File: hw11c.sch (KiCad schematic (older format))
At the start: 68 parts, among them Q1 KX-7_12MHZ, SW1 BUTT1, SW2 BUTT2, X1 ~RESET, X10 PIO2.8, X11 PIO1.4, X12 ADC3, X13 PIO0.8, X14 PIO0.9, X15 MAT0, X16 PIO0.6, X17 PIO0.7, X2 SWCLK, X3 SWDIO, X4 SSEL1, X5 SCK1, X6 MISO1, X7 MOSI1, X8 PIO2.6, X9 PIO2.7

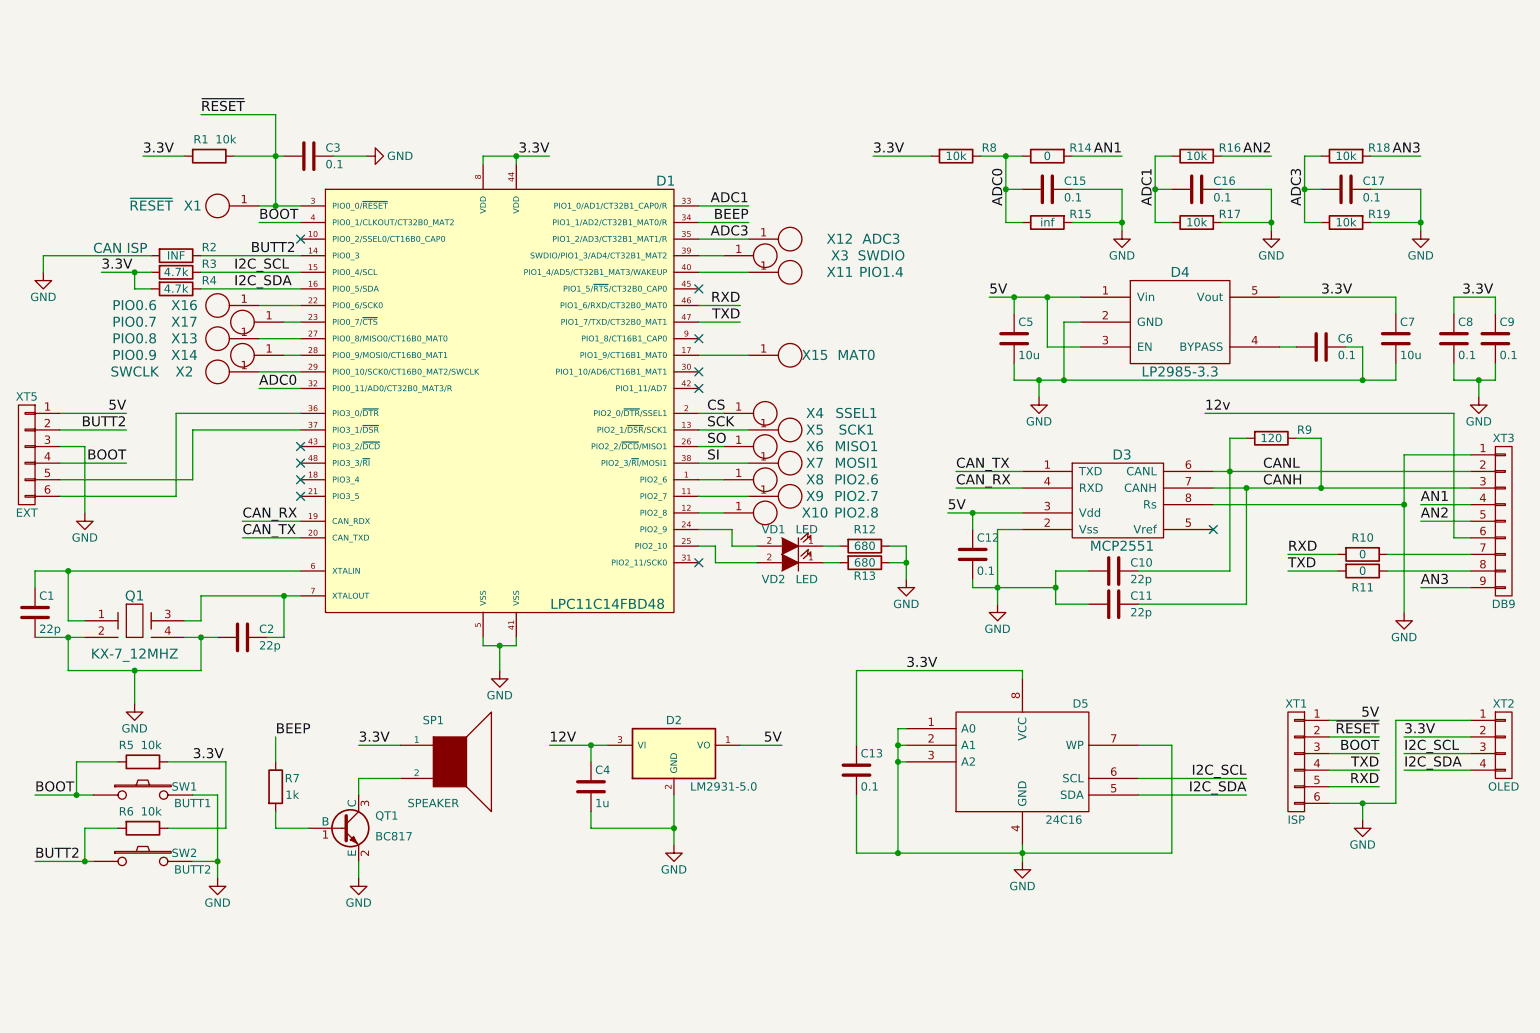
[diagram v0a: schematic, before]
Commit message: Add fault-tolerance CAN PHY: TJA1055. Version of board 2.1.
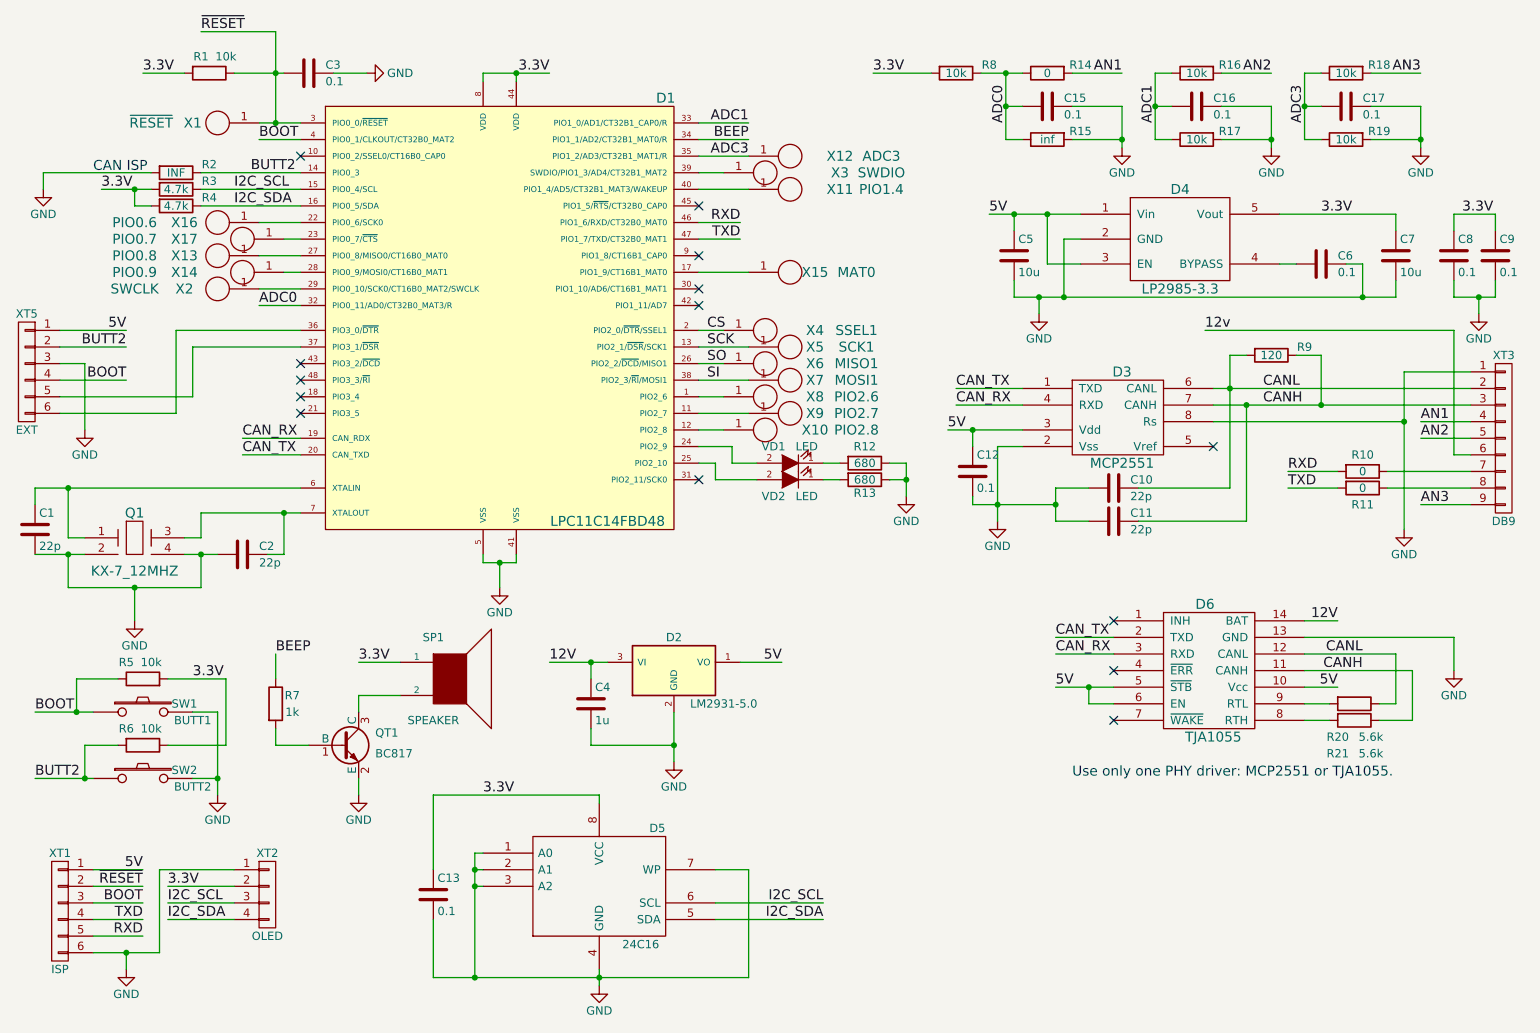
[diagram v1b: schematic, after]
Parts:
- added D6: TJA1055, libs:SOIC-14_N, symbol TJA1055
- added R20, R21: 5.6k, libs:R_0603, symbol R
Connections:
- net 12V: now also D6.14 (BAT)
- net 5V: now also D6.10 (Vcc), D6.5 (~STB), D6.6 (EN)
- net CANH: now also D6.11 (CANH), R21.1
- net CANL: now also D6.12 (CANL), R20.1
- net CAN_RX: now also D6.3 (RXD)
- net CAN_TX: now also D6.2 (TXD)
- net GND: now also D6.13 (GND)
- new net: D6.8 (RTH), R21.2
- new net: D6.9 (RTL), R20.2
- no-connect marks 11 -> 14
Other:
- note added: "Use only one PHY driver: MCP2551 or TJA1055."
- moved on the sheet: C1, C10, C11, C12, C13, C15, C16, C17, C2, C3, C4, C5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
